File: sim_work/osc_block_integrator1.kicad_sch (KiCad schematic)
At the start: 6 parts, among them U2 LM4562

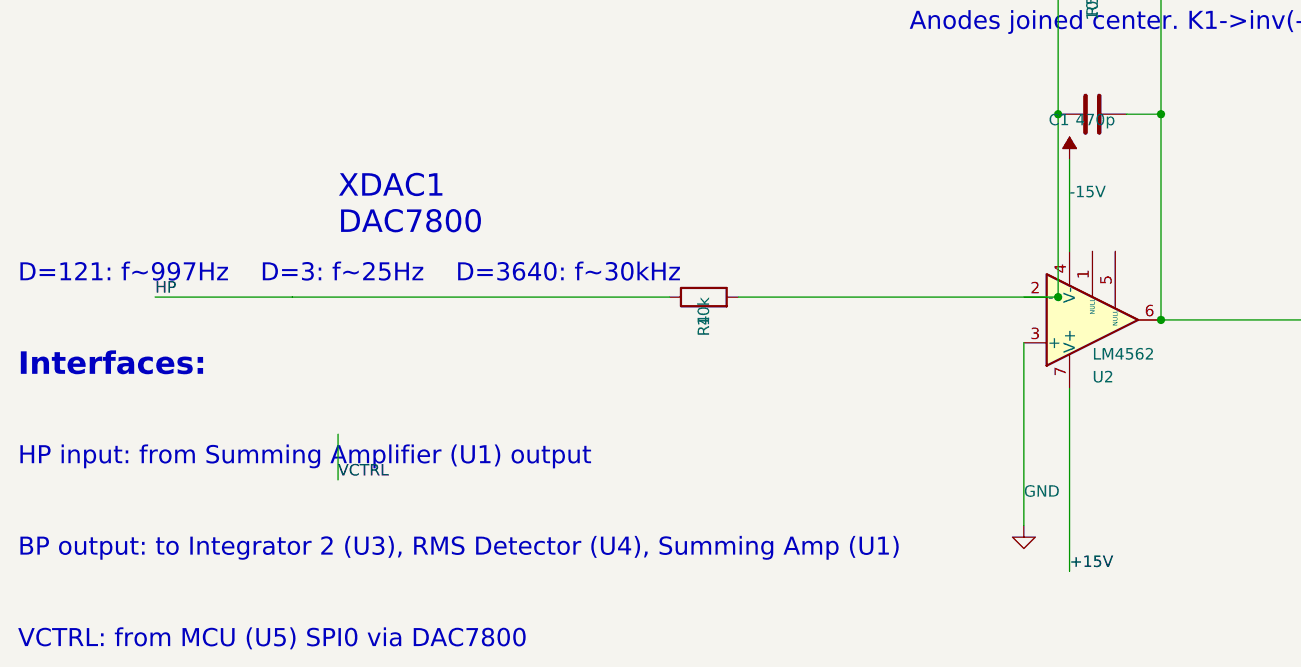
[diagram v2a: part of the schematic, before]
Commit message: Add comparison mode, fix SimGUI subprocess popups, DAC7800 IC boxes
- SimGUI: fix Python path detection (FindPython searches Python312/313/311)
- SimGUI: suppress console popup windows (CREATE_NO_WINDOW for subprocess)
- SimGUI: add Comparison project (MDAC vs Analog oscillator side-by-side)
- SimGUI: fix async wrapping (direct await instead of Task.Run)
- Pipeline: draw DAC7800 as proper IC box with pin labels (VREF/IOUT/VCTRL)
- Pipeline: fix electrometer_362 layout (spacing, junction dots at T-junctions)
- Pipeline: fix summing amp gain annotations (BP=-0.455, not -2.2)
- Pipeline: add analog_osc command for friend's SVF oscillator simulation
- Docs: comparison_guide.md, updated README and PROJECT tracker

Co-Authored-By: Claude Opus 4.6 <noreply@anthropic.com>
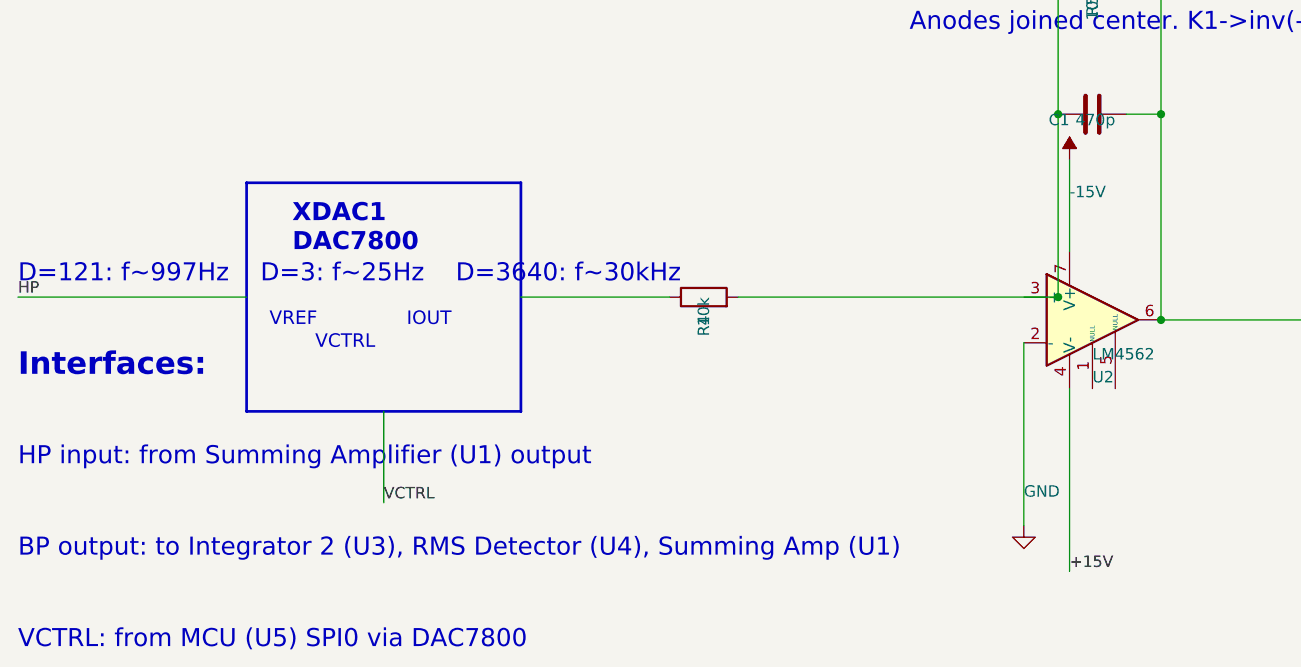
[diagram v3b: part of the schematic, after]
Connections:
- net +15V: now also U2.4 (V-); no longer U2.7 (V+)
- net -15V: now also U2.7 (V+); no longer U2.4 (V-)
- net GND: now also U2.2 (-); no longer U2.3 (+)
- net HP: no longer R4.1
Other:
- note added: "IOUT"
- note added: "VCTRL"
- note added: "VREF"
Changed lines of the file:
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@@
 		(lib_id "LM741:LM741")
 		(at 139.7 152.4 0)
-		(mirror x)
 		(unit 1)
 		(exclude_from_sim no)
@@
 		(instances
 			(project "Oscillator - Integrator 1"
-				(path "/0aa0564e-5a8b-4527-900e-69c0f4e778f3"
+				(path "/1cc531ed-13bc-415a-8cf0-396766e5bba2"
 					(reference "U2")
 					(unit 1)
@@
 		(instances
 			(project "Oscillator - Integrator 1"
-				(path "/0aa0564e-5a8b-4527-900e-69c0f4e778f3"
+				(path "/1cc531ed-13bc-415a-8cf0-396766e5bba2"
 					(reference "R4")
 					(unit 1)
@@
 		(instances
 			(project "Oscillator - Integrator 1"
-				(path "/0aa0564e-5a8b-4527-900e-69c0f4e778f3"
+				(path "/1cc531ed-13bc-415a-8cf0-396766e5bba2"
 					(reference "C1")
 					(unit 1)
@@
 		(instances
 			(project "Oscillator - Integrator 1"
-				(path "/0aa0564e-5a8b-4527-900e-69c0f4e778f3"
+				(path "/1cc531ed-13bc-415a-8cf0-396766e5bba2"
 					(reference "R5")
 					(unit 1)
@@
 		(instances
 			(project "Oscillator - Integrator 1"
-				(path "/0aa0564e-5a8b-4527-900e-69c0f4e778f3"
+				(path "/1cc531ed-13bc-415a-8cf0-396766e5bba2"
 					(reference "D1")
 					(unit 1)
@@
 		(instances
 			(project "Oscillator - Integrator 1"
-				(path "/0aa0564e-5a8b-4527-900e-69c0f4e778f3"
+				(path "/1cc531ed-13bc-415a-8cf0-396766e5bba2"
 					(reference "D2")
 					(unit 1)
@@
 		(instances
 			(project "Oscillator - Integrator 1"
-				(path "/0aa0564e-5a8b-4527-900e-69c0f4e778f3"
+				(path "/1cc531ed-13bc-415a-8cf0-396766e5bba2"
 					(reference "#PWR001")
 					(unit 1)
@@
 		(instances
 			(project "Oscillator - Integrator 1"
-				(path "/0aa0564e-5a8b-4527-900e-69c0f4e778f3"
+				(path "/1cc531ed-13bc-415a-8cf0-396766e5bba2"
 					(reference "#PWR002")
 					(unit 1)
@@
 	(wire
 		(pts
-			(xy 35.56 149.86) (xy 50.8 149.86)
-		)
-		(stroke
-			(width 0)
-			(type default)
-		)
-	)
-	(wire
-		(pts
-			(xy 50.8 149.86) (xy 92.71 149.86)
-		)
-		(stroke
-			(width 0)
-			(type default)
-		)
-	)
-	(wire
-		(pts
-			(xy 55.88 170.18) (xy 55.88 165.1)
+			(xy 20.32 149.86) (xy 45.72 149.86)
+		)
+		(stroke
+			(width 0)
+			(type default)
+		)
+	)
+	(wire
+		(pts
+			(xy 76.2 149.86) (xy 92.71 149.86)
+		)
+		(stroke
+			(width 0)
+			(type default)
+		)
+	)
+	(wire
+		(pts
+			(xy 60.96 162.56) (xy 60.96 172.72)
 		)
 		(stroke
@@
 	)
 	(label "HP"
-		(at 35.56 149.86 0)
+		(at 20.32 149.86 0)
 		(effects
 			(font
@@
 	)
 	(label "VCTRL"
-		(at 55.88 170.18 0)
+		(at 60.96 172.72 0)
 		(effects
 			(font
@@
 		)
 	)
+	(rectangle
+		(start 45.72 137.16)
+		(end 76.2 162.56)
+		(stroke
+			(width 0.3)
+			(type solid)
+		)
+		(fill
+			(type none)
+		)
+	)
 	(text "INTEGRATOR 1: HP -> BP (U2 + XDAC1)"
 		(exclude_from_sim no)
@@
 	(text "XDAC1\nDAC7800"
 		(exclude_from_sim no)
-		(at 55.88 139.7 0.0000)
-		(effects
-			(font
-				(size 2.5 2.5)
-			)
-			(justify left)
+		(at 50.8 142.24 0.0000)
+		(effects
+			(font
+				(size 2 2)
+				(bold yes)
+			)
+			(justify left)
+		)
+	)
+	(text "VREF"
+		(exclude_from_sim no)
+		(at 48.26 152.4 0.0000)
+		(effects
+			(font
+				(size 1.5 1.5)
+			)
+			(justify left)
+		)
+	)
+	(text "IOUT"
+		(exclude_from_sim no)
+		(at 63.5 152.4 0.0000)
+		(effects
+			(font
+				(size 1.5 1.5)
+			)
+			(justify left)
+		)
+	)
+	(text "VCTRL"
+		(exclude_from_sim no)
+		(at 53.34 154.94 0.0000)
+		(effects
+			(font
+				(size 1.5 1.5)
+			)
+			(justify left)
